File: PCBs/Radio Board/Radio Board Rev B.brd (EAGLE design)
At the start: 160 x 100 mm, 2 parts

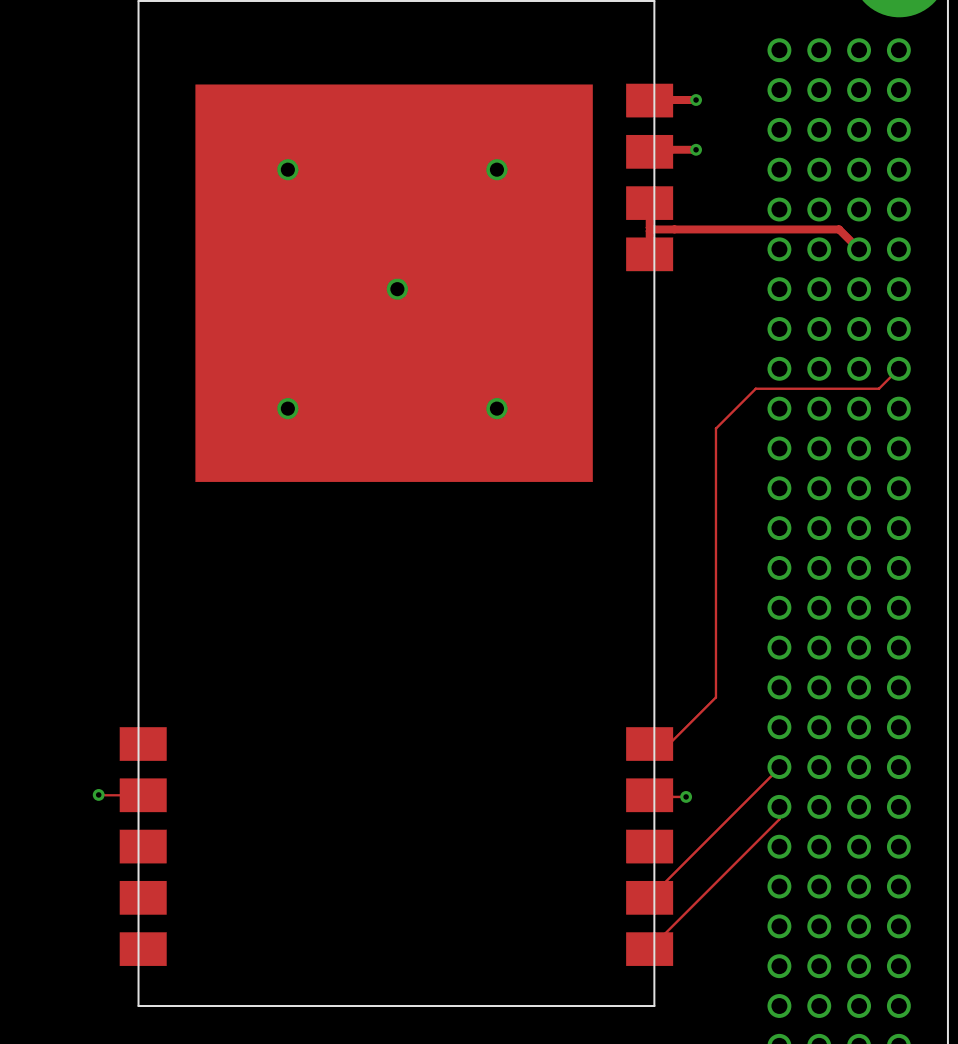
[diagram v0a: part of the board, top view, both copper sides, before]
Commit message: Added bypass caps to radio
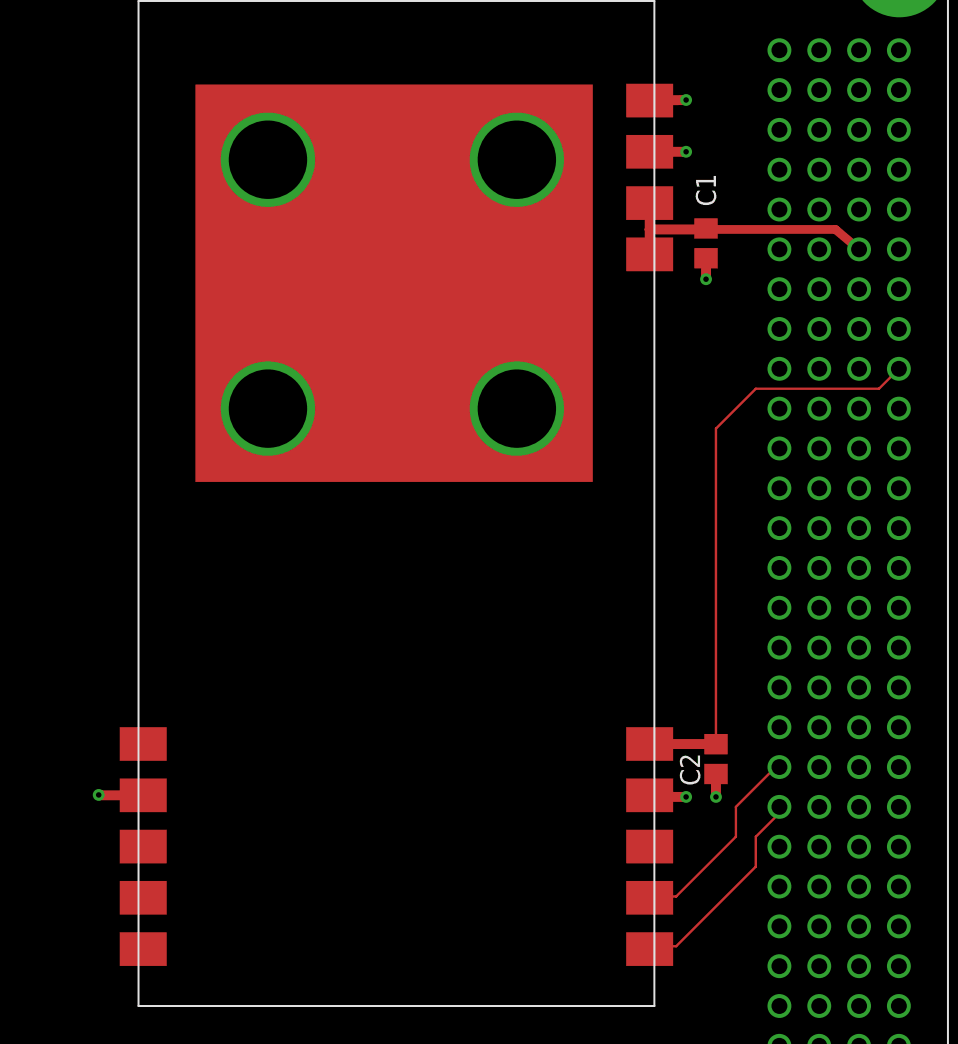
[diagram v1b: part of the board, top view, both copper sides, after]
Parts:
- added C1: 1uF, resistor:C0805
- added C2: 0.1uF, resistor:C0805
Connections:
- net GND: now also C1.2, C2.2
- net SW3: now also C1.1
- net SW8: now also C2.1
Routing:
- net SW8: track 36.0 -> 37.6 mm
- net GND: track 11.3 -> 12.8 mm, vias 9 -> 10
- net LITHIUM_RX_UART: track 11.8 -> 12.8 mm
- net LITHIUM_TX_UART: track 12.5 -> 13.4 mm
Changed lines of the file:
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@@
 <?xml version="1.0" encoding="utf-8"?>
 <!DOCTYPE eagle SYSTEM "eagle.dtd">
-<eagle version="9.0.1">
+<eagle version="9.1.0">
 <drawing>
 <settings>
-<setting alwaysvectorfont="no"/>
+<setting alwaysvectorfont="yes"/>
 <setting verticaltext="up"/>
 </settings>
@@
 <param name="checkStop" value="0"/>
 <param name="checkValues" value="0"/>
+<param name="checkNames" value="1"/>
+<param name="checkWireStubs" value="1"/>
+<param name="checkPolygonWidth" value="0"/>
 <param name="useDiameter" value="13"/>
 <param name="maxErrors" value="50"/>
@@
 <element name="U$1" library="Cubesat" package="LI-1" value="LITHIUM" x="43.815" y="17.78"/>
 <element name="U$2" library="Cubesat" package="PC104" value="PC104" x="2.54" y="2.54"/>
+<element name="C1" library="resistor" library_urn="urn:adsk.eagle:library:348" package="C0805" package3d_urn="urn:adsk.eagle:package:26137/1" value="1uF" x="80.01" y="66.421" smashed="yes" rot="R270">
+<attribute name="NAME" x="79.375" y="70.866" size="1.27" layer="25" rot="R270"/>
+<attribute name="VALUE" x="81.28" y="70.866" size="1.27" layer="27" rot="R270"/>
+</element>
+<element name="C2" library="resistor" library_urn="urn:adsk.eagle:library:348" package="C0805" package3d_urn="urn:adsk.eagle:package:26137/1" value="0.1uF" x="80.645" y="33.528" smashed="yes" rot="R270">
+<attribute name="NAME" x="78.359" y="33.909" size="1.27" layer="25" rot="R270"/>
+<attribute name="VALUE" x="81.915" y="36.068" size="1.27" layer="27" rot="R270"/>
+</element>
 </elements>
 <signals>
@@
 <contactref element="U$1" pad="GND1"/>
 <contactref element="U$1" pad="GND2"/>
-<contactref element="U$1" pad="RF_GND2"/>
-<contactref element="U$1" pad="RF_GND3"/>
-<contactref element="U$1" pad="RF_GND1"/>
 <wire x1="76.415" y1="31.22" x2="76.52" y2="31.115" width="0.1524" layer="1"/>
-<wire x1="76.52" y1="31.115" x2="78.74" y2="31.115" width="0.1524" layer="1"/>
+<wire x1="76.52" y1="31.115" x2="78.74" y2="31.115" width="0.635" layer="1"/>
 <via x="78.74" y="31.115" extent="1-16" drill="0.35"/>
 <wire x1="44.115" y1="31.22" x2="44.22" y2="31.115" width="0.1524" layer="1"/>
@@
 <contactref element="U$2" pad="P$84"/>
 <contactref element="U$2" pad="P$100"/>
-<wire x1="44.115" y1="31.22" x2="41.38" y2="31.22" width="0.1524" layer="1"/>
-<wire x1="41.38" y1="31.22" x2="41.275" y2="31.242" width="0.1524" layer="1"/>
 <via x="41.275" y="31.242" extent="1-16" drill="0.35"/>
-<via x="60.325" y="63.5" extent="1-16" drill="0.9"/>
-<via x="66.675" y="55.88" extent="1-16" drill="0.9"/>
-<via x="66.675" y="71.12" extent="1-16" drill="0.9"/>
-<via x="53.34" y="71.12" extent="1-16" drill="0.9"/>
-<via x="53.34" y="55.88" extent="1-16" drill="0.9"/>
+<via x="67.945" y="55.88" extent="1-16" drill="4.999990625"/>
+<via x="67.945" y="71.755" extent="1-16" drill="4.999990625"/>
+<via x="52.07" y="71.755" extent="1-16" drill="4.999990625"/>
+<via x="52.07" y="55.88" extent="1-16" drill="4.999990625"/>
 <polygon width="0.1524" layer="16">
 <vertex x="1.27" y="93.98"/>
@@
 <vertex x="1.27" y="1.905"/>
 </polygon>
-<wire x1="76.415" y1="75.53" x2="76.45" y2="75.565" width="0.508" layer="1"/>
-<wire x1="76.45" y1="75.565" x2="79.375" y2="75.565" width="0.508" layer="1"/>
-<wire x1="76.415" y1="72.26" x2="76.545" y2="72.39" width="0.508" layer="1"/>
-<wire x1="76.545" y1="72.39" x2="79.375" y2="72.39" width="0.508" layer="1"/>
-<via x="79.375" y="75.565" extent="1-16" drill="0.35"/>
-<via x="79.375" y="72.39" extent="1-16" drill="0.35"/>
-<wire x1="60.325" y1="63.5" x2="60.115" y2="63.88" width="0" layer="19" extent="1-1"/>
+<wire x1="41.275" y1="31.242" x2="41.297" y2="31.22" width="0.508" layer="1"/>
+<wire x1="41.297" y1="31.22" x2="44.115" y2="31.22" width="0.635" layer="1"/>
+<contactref element="C2" pad="2"/>
+<contactref element="C1" pad="2"/>
+<contactref element="U$1" pad="RF_GND1"/>
+<contactref element="U$1" pad="RF_GND3"/>
+<contactref element="U$1" pad="RF_GND2"/>
+<wire x1="80.645" y1="32.578" x2="80.645" y2="31.115" width="0.635" layer="1"/>
+<via x="80.645" y="31.115" extent="1-16" drill="0.35"/>
+<wire x1="80.01" y1="65.471" x2="80.01" y2="64.135" width="0.635" layer="1"/>
+<via x="80.01" y="64.135" extent="1-16" drill="0.35"/>
+<wire x1="76.415" y1="72.26" x2="78.74" y2="72.263" width="0.635" layer="1"/>
+<wire x1="76.415" y1="75.53" x2="78.74" y2="75.565" width="0.635" layer="1"/>
+<via x="78.74" y="75.565" extent="1-16" drill="0.35"/>
+<via x="78.74" y="72.263" extent="1-16" drill="0.35"/>
+<wire x1="67.945" y1="71.755" x2="60.115" y2="63.88" width="0" layer="19" extent="1-1"/>
 </signal>
 <signal name="SW3">
@@
 <contactref element="U$1" pad="V_AMP1"/>
 <contactref element="U$1" pad="V_AMP2"/>
-<wire x1="89.77121875" y1="66.04" x2="88.50121875" y2="67.31" width="0.508" layer="1"/>
-<wire x1="88.50121875" y1="67.31" x2="78.005" y2="67.31" width="0.508" layer="1"/>
-<wire x1="78.005" y1="67.31" x2="78.005" y2="67.4" width="0.1524" layer="1"/>
-<wire x1="78.005" y1="67.31" x2="76.5175" y2="67.31" width="0.508" layer="1"/>
-<wire x1="76.5175" y1="67.31" x2="76.415" y2="67.4125" width="0.508" layer="1"/>
-<wire x1="76.415" y1="67.4125" x2="76.415" y2="68.99" width="0.508" layer="1"/>
-<wire x1="76.5175" y1="67.31" x2="76.415" y2="67.2075" width="0.508" layer="1"/>
-<wire x1="76.415" y1="67.2075" x2="76.415" y2="65.72" width="0.508" layer="1"/>
+<wire x1="76.415" y1="68.99" x2="76.415" y2="67.31" width="0.635" layer="1"/>
+<wire x1="76.415" y1="67.31" x2="76.415" y2="65.72" width="0.635" layer="1"/>
+<contactref element="C1" pad="1"/>
+<wire x1="76.415" y1="67.31" x2="79.949" y2="67.31" width="0.635" layer="1"/>
+<wire x1="79.949" y1="67.31" x2="80.01" y2="67.371" width="0.635" layer="1"/>
+<wire x1="89.77121875" y1="66.04" x2="88.265" y2="67.31" width="0.5588" layer="1"/>
+<wire x1="88.265" y1="67.31" x2="79.949" y2="67.31" width="0.5588" layer="1"/>
 </signal>
 <signal name="SW8">
@@
 <wire x1="91.04121875" y1="57.15" x2="83.185" y2="57.15" width="0.1524" layer="1"/>
 <wire x1="83.185" y1="57.15" x2="80.645" y2="54.61" width="0.1524" layer="1"/>
-<wire x1="80.645" y1="37.465" x2="77.47" y2="34.29" width="0.1524" layer="1"/>
-<wire x1="77.47" y1="34.29" x2="77.27" y2="34.49" width="0.1524" layer="1"/>
-<wire x1="77.27" y1="34.49" x2="76.415" y2="34.49" width="0.1524" layer="1"/>
-<wire x1="80.645" y1="54.61" x2="80.645" y2="37.465" width="0.1524" layer="1"/>
+<contactref element="C2" pad="1"/>
+<wire x1="76.415" y1="34.49" x2="80.633" y2="34.49" width="0.635" layer="1"/>
+<wire x1="80.633" y1="34.49" x2="80.645" y2="34.478" width="0.635" layer="1"/>
+<wire x1="80.645" y1="54.61" x2="80.645" y2="34.502" width="0.1524" layer="1"/>
+<wire x1="80.645" y1="34.502" x2="80.633" y2="34.49" width="0.1524" layer="1"/>
 </signal>
 <signal name="LITHIUM_TX_UART">
 <contactref element="U$1" pad="TX_UART"/>
 <contactref element="U$2" pad="P$39"/>
-<wire x1="76.415" y1="21.41" x2="84.69121875" y2="29.68621875" width="0.1524" layer="1"/>
-<wire x1="84.69121875" y1="29.68621875" x2="84.69121875" y2="30.48" width="0.1524" layer="1"/>
+<wire x1="76.415" y1="21.41" x2="76.595" y2="21.59" width="0.1524" layer="1"/>
+<wire x1="76.595" y1="21.59" x2="78.105" y2="21.59" width="0.1524" layer="1"/>
+<wire x1="78.105" y1="21.59" x2="83.185" y2="26.67" width="0.1524" layer="1"/>
+<wire x1="83.185" y1="26.67" x2="83.185" y2="28.575" width="0.1524" layer="1"/>
+<wire x1="83.185" y1="28.575" x2="84.69121875" y2="30.08121875" width="0.1524" layer="1"/>
+<wire x1="84.69121875" y1="30.08121875" x2="84.69121875" y2="30.48" width="0.1524" layer="1"/>
 </signal>
 <signal name="LITHIUM_RX_UART">
 <contactref element="U$1" pad="RX_UART"/>
 <contactref element="U$2" pad="P$37"/>
-<wire x1="76.415" y1="24.68" x2="84.69121875" y2="32.95621875" width="0.1524" layer="1"/>
-<wire x1="84.69121875" y1="32.95621875" x2="84.69121875" y2="33.02" width="0.1524" layer="1"/>
+<wire x1="76.415" y1="24.68" x2="76.5" y2="24.765" width="0.1524" layer="1"/>
+<wire x1="76.5" y1="24.765" x2="78.105" y2="24.765" width="0.1524" layer="1"/>
+<wire x1="78.105" y1="24.765" x2="81.915" y2="28.575" width="0.1524" layer="1"/>
+<wire x1="81.915" y1="28.575" x2="81.915" y2="30.48" width="0.1524" layer="1"/>
+<wire x1="81.915" y1="30.48" x2="84.455" y2="33.02" width="0.1524" layer="1"/>
+<wire x1="84.455" y1="33.02" x2="84.69121875" y2="33.02" width="0.1524" layer="1"/>
 </signal>
 </signals>
+<mfgpreviewcolors>
+<mfgpreviewcolor name="soldermaskcolor" color="0xC8008000"/>
+<mfgpreviewcolor name="silkscreencolor" color="0xFFFEFEFE"/>
+<mfgpreviewcolor name="backgroundcolor" color="0xFF282828"/>
+<mfgpreviewcolor name="coppercolor" color="0xFFFFBF00"/>
+<mfgpreviewcolor name="substratecolor" color="0xFF786E46"/>
+</mfgpreviewcolors>
 </board>
 </drawing>
+<compatibility>
+<note version="8.2" severity="warning">
+Since Version 8.2, EAGLE supports online libraries. The ids
+of those online libraries will not be understood (or retained)
+with this version.
+</note>
+<note version="8.3" severity="warning">
+Since Version 8.3, EAGLE supports URNs for individual library
+assets (packages, symbols, and devices). The URNs of those assets
+will not be understood (or retained) with this version.
+</note>
+<note version="8.3" severity="warning">
+Since Version 8.3, EAGLE supports the association of 3D packages
+with devices in libraries, schematics, and board files. Those 3D
+packages will not be understood (or retained) with this version.
+</note>
+</compatibility>
 </eagle>

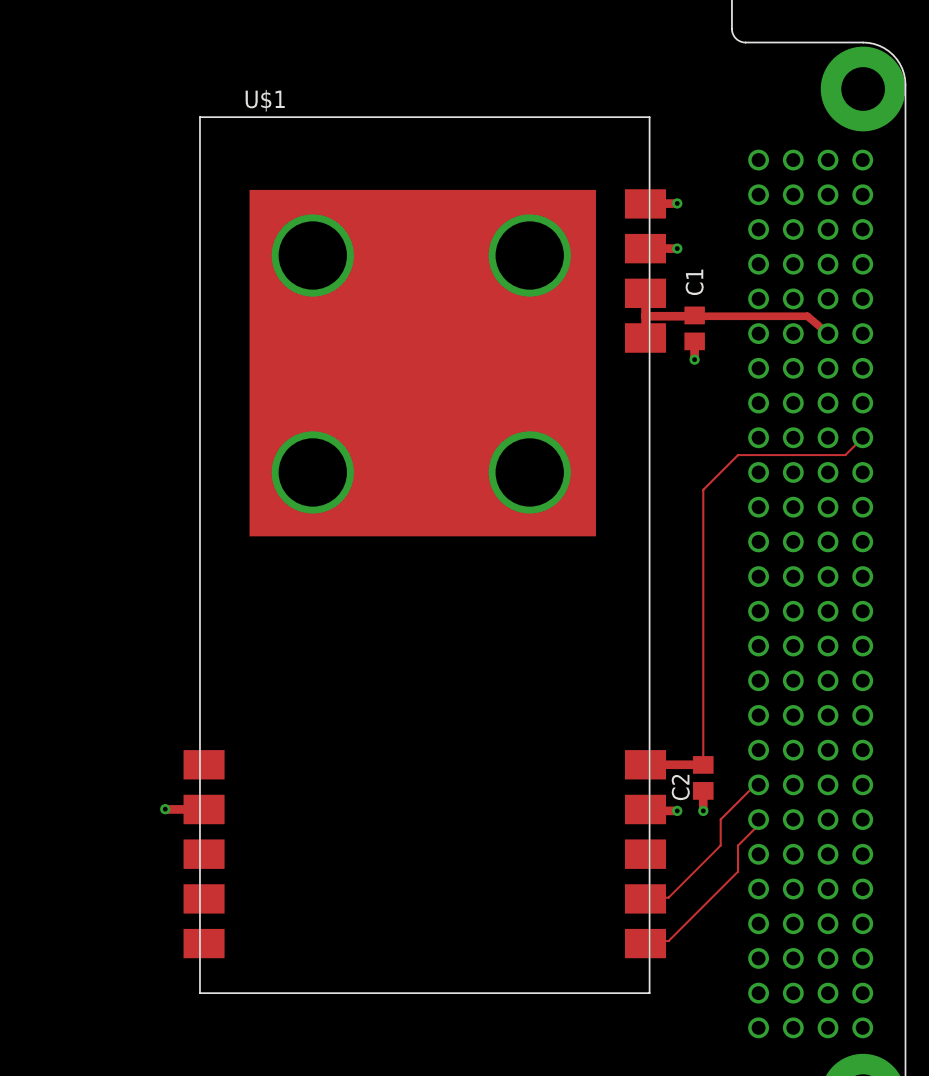
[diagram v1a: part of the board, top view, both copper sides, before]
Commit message: Add temp sensors to GPS and Radio boards
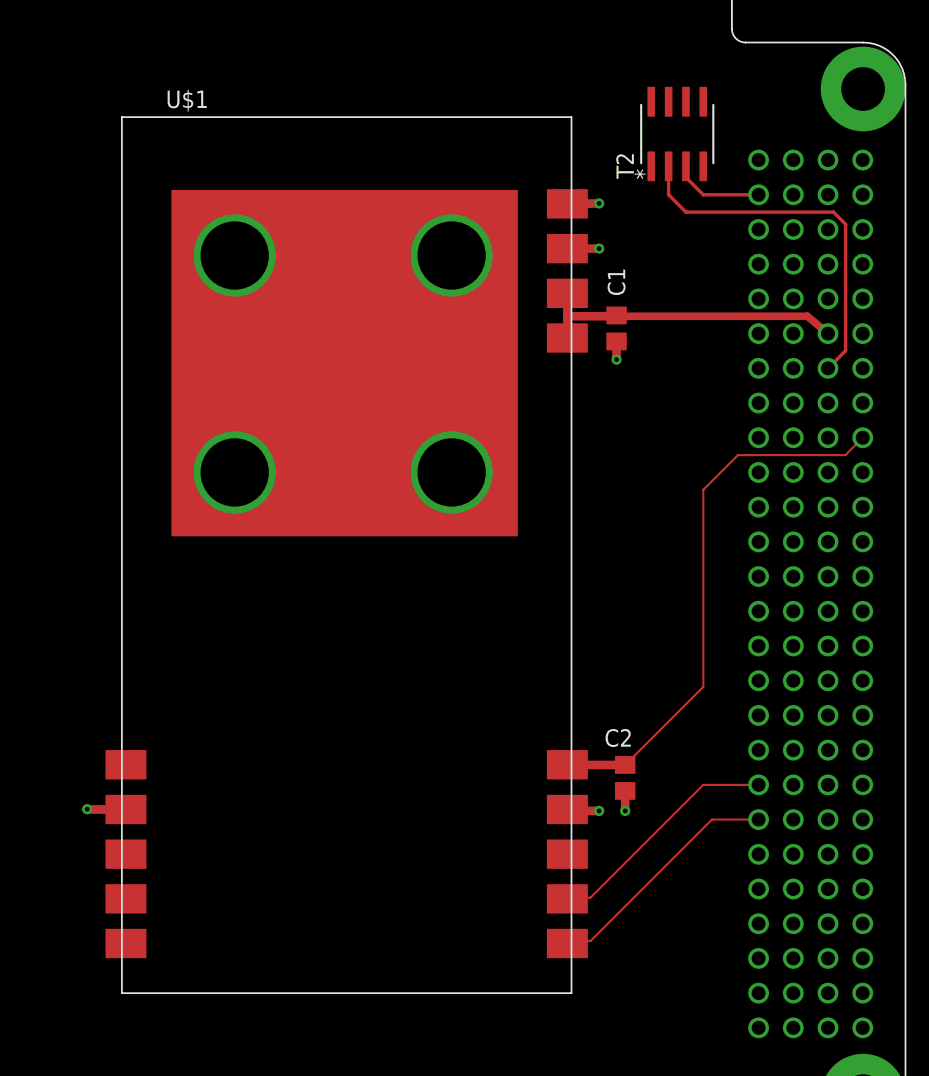
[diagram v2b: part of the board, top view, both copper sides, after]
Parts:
- added T2: AD590KRZ, AD590KRZ:R_8
- moved C1 5.72 mm to (74.3, 66.4)
- moved U$1 5.71 mm to (38.1, 17.8)
- moved C2 5.71 mm to (74.9, 33.5)
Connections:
- new net N$1: T2.3, U$2.P$3
- new net SW5: T2.2, U$2.P$65
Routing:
- net SW5: track 0.00 -> 27.0 mm
- net N$1: track 0.00 -> 6.66 mm
- net SW3: track 17.2 -> 22.9 mm
- net LITHIUM_RX_UART: track 12.8 -> 17.4 mm
- net LITHIUM_TX_UART: track 13.4 -> 17.7 mm
- net SW8: track 37.6 -> 40.0 mm
